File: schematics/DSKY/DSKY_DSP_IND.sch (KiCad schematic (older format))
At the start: 87 parts, among them Q10 Q_NPN, Q11 Q_NPN, Q12 Q_NPN, Q13 Q_NPN, Q14 Q_NPN, Q15 Q_NPN, Q16 Q_NPN, Q3 Q_NPN, Q4 Q_NPN, Q5 Q_NPN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

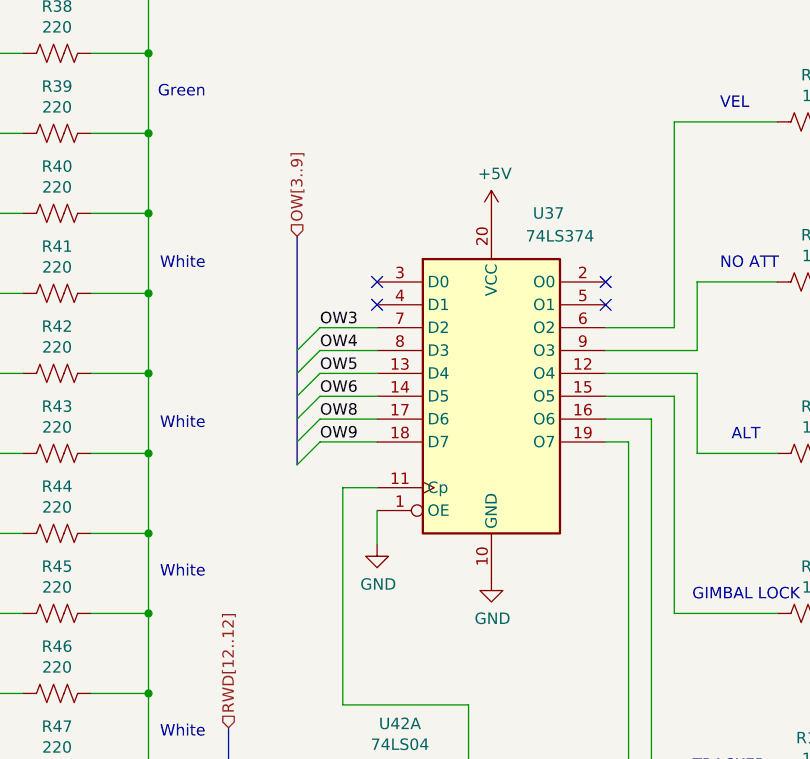
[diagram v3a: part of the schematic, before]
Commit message: Simplified reset lines.
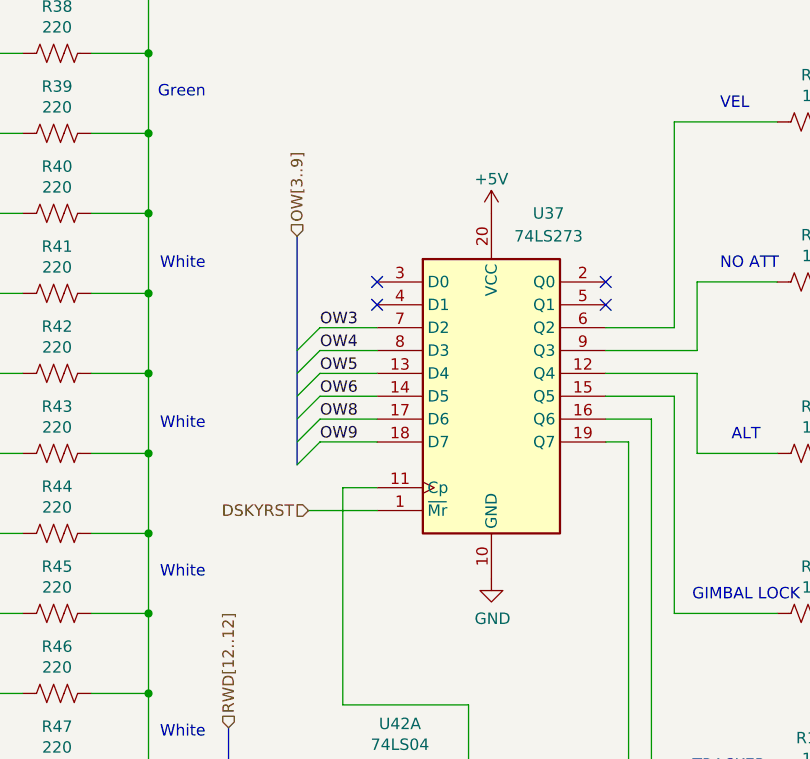
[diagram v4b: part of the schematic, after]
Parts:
- removed U37: 74LS374, symbol 74xx:74LS374
- added U37: 74LS273, symbol 74xx:74LS273
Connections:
- net +5V: now also U37.20 (VCC)
- net GND: now also U37.10 (GND)
- net OW3: now also U37.7 (D2)
- net OW4: now also U37.8 (D3)
- net OW5: now also U37.13 (D4)
- net OW6: now also U37.14 (D5)
- net OW8: now also U37.17 (D6)
- net OW9: now also U37.18 (D7)
- net PROG: now also U37.19 (Q7)
- net at U42.2: now also U37.11 (Cp)
- net at R8.1: now also U37.12 (Q4)
- net at R9.1: now also U37.15 (Q5)
- net at R10.1: now also U37.16 (Q6)
- net at R6.1: now also U37.6 (Q2)
- net at R7.1: now also U37.9 (Q3)
- new net DSKYRST: U37.1 (~Mr)
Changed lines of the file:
@@
 	1    0    0    -1
 $EndComp
-Wire Wire Line
-	6000 4000 6000 4150
 $Comp
 L power:+5V #PWR?
@@
 AR Path="/60F98A64/68A00B2E/68A8928A" Ref="#PWR0116"  Part="1"
 F 0 "#PWR0116" H 6500 2550 50  0001 C CNN
-F 1 "+5V" H 6515 2873 50  0000 C CNN
+F 1 "+5V" H 6500 2850 50  0000 C CNN
 F 2 "" H 6500 2700 50  0001 C CNN
 F 3 "" H 6500 2700 50  0001 C CNN
@@
 F 3 "" H 6500 4300 50  0001 C CNN
 	1    6500 4300
-	1    0    0    -1
-$EndComp
-$Comp
-L 74xx:74LS374 U?
-U 1 1 68A8927E
-P 6500 3500
-AR Path="/60F98A64/637944C1/68A8927E" Ref="U?"  Part="1"
-AR Path="/60F98A64/64844A8A/68A8927E" Ref="U?"  Part="1"
-AR Path="/60F98A64/63794472/68A8927E" Ref="U?"  Part="1"
-AR Path="/60F98A64/68A00B2E/68A8927E" Ref="U37"  Part="1"
-F 0 "U37" H 6750 4300 50  0000 C CNN
-F 1 "74LS374" H 6800 4200 50  0000 C CNN
-F 2 "" H 6500 3500 50  0001 C CNN
-F 3 "http://www.ti.com/lit/gpn/sn74LS374" H 6500 3500 50  0001 C CNN
-	1    6500 3500
 	1    0    0    -1
 $EndComp
@@
 NoConn ~ 6000 3100
 $Comp
-L power:GND #PWR?
-U 1 1 635E6D82
-P 6000 4150
-AR Path="/60F98A64/637944C1/635E6D82" Ref="#PWR?"  Part="1"
-AR Path="/60F98A64/64844A8A/635E6D82" Ref="#PWR?"  Part="1"
-AR Path="/60F98A64/63794472/635E6D82" Ref="#PWR?"  Part="1"
-AR Path="/60F98A64/68A00B2E/635E6D82" Ref="#PWR0110"  Part="1"
-F 0 "#PWR0110" H 6000 3900 50  0001 C CNN
-F 1 "GND" H 6005 3977 50  0000 C CNN
-F 2 "" H 6000 4150 50  0001 C CNN
-F 3 "" H 6000 4150 50  0001 C CNN
-	1    6000 4150
-	1    0    0    -1
-$EndComp
-$Comp
 L 74xx:74LS04 U42
 U 1 1 635EB464
@@
 Wire Wire Line
 	6400 4850 6400 5250
+$Comp
+L 74xx:74LS273 U37
+U 1 1 638DD418
+P 6500 3500
+F 0 "U37" H 6750 4300 50  0000 C CNN
+F 1 "74LS273" H 6750 4200 50  0000 C CNN
+F 2 "" H 6500 3500 50  0001 C CNN
+F 3 "http://www.ti.com/lit/gpn/sn74LS273" H 6500 3500 50  0001 C CNN
+	1    6500 3500
+	1    0    0    -1
+$EndComp
+Text HLabel 5700 4000 0    50   Input ~ 0
+DSKYRST
+Wire Wire Line
+	6000 4000 5700 4000
 Wire Bus Line
 	5350 4950 5350 5400

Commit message: Added DSKY test schematic
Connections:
- net PROG: no longer names the net of R11.1, U37.19 (Q7)
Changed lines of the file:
@@
 $Descr A 11000 8500
 encoding utf-8
-Sheet 5 11
+Sheet 5 12
 Title ""
 Date ""
@@
 Text Notes 2400 6600 2    50   ~ 0
 Flash V/N
-Wire Wire Line
-	7100 5900 7100 6150
-Wire Wire Line
-	7100 6150 7350 6150
-Connection ~ 7100 5900
-Text HLabel 7350 6150 2    50   Output ~ 0
-PROG
 NoConn ~ 7000 3000
 Connection ~ 10200 1950

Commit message: DSKY Redesign
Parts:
- removed D31, D32: LED, symbol Device:LED
- removed Q16: Q_NPN, symbol Device:Q_NPN_BCE
- removed R35: 1k, symbol Device:R_US
- removed R50, R51: 220, symbol Device:R_US
- added unit 3 of U19
- renumbered U42 to U19, U40 to U59
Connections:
- net PARALM: now also U59.13; no longer U59.1
- net STBY: now also U19.5; no longer U59.2
- net at R28.1: now also U59.11; no longer U59.3
- new net: U19.6, U59.12
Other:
- note removed: "Flash V/N"
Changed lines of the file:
@@
 $Descr A 11000 8500
 encoding utf-8
-Sheet 5 12
+Sheet 7 15
 Title ""
 Date ""
@@
 Text Notes 5050 5700 0    50   ~ 0
 Yellow
-$Comp
-L Device:Q_NPN_BCE Q?
-U 1 1 66B1B9DB
-P 3250 6650
-AR Path="/60F98A64/64844A8A/66B1B9DB" Ref="Q?"  Part="1"
-AR Path="/60F98A64/68A00B2E/66B1B9DB" Ref="Q16"  Part="1"
-F 0 "Q16" H 3441 6696 50  0000 L CNN
-F 1 "Q_NPN" H 3441 6605 50  0000 L CNN
-F 2 "" H 3450 6750 50  0001 C CNN
-F 3 "~" H 3250 6650 50  0001 C CNN
-	1    3250 6650
-	1    0    0    -1
-$EndComp
-$Comp
-L Device:R_US R?
-U 1 1 66B1B9E1
-P 2700 6650
-AR Path="/60F98A64/64844A8A/66B1B9E1" Ref="R?"  Part="1"
-AR Path="/60F98A64/68A00B2E/66B1B9E1" Ref="R35"  Part="1"
-F 0 "R35" V 2905 6650 50  0000 C CNN
-F 1 "1k" V 2814 6650 50  0000 C CNN
-F 2 "" V 2740 6640 50  0001 C CNN
-F 3 "~" H 2700 6650 50  0001 C CNN
-	1    2700 6650
-	0    -1   -1   0
-$EndComp
-$Comp
-L Device:LED D?
-U 1 1 66B1B9E7
-P 4150 6250
-AR Path="/60F98A64/64844A8A/66B1B9E7" Ref="D?"  Part="1"
-AR Path="/60F98A64/68A00B2E/66B1B9E7" Ref="D31"  Part="1"
-F 0 "D31" H 4143 6467 50  0000 C CNN
-F 1 "LED" H 4143 6376 50  0000 C CNN
-F 2 "" H 4150 6250 50  0001 C CNN
-F 3 "~" H 4150 6250 50  0001 C CNN
-	1    4150 6250
-	1    0    0    -1
-$EndComp
-$Comp
-L Device:LED D?
-U 1 1 66B1B9ED
-P 4150 6650
-AR Path="/60F98A64/64844A8A/66B1B9ED" Ref="D?"  Part="1"
-AR Path="/60F98A64/68A00B2E/66B1B9ED" Ref="D32"  Part="1"
-F 0 "D32" H 4143 6867 50  0000 C CNN
-F 1 "LED" H 4143 6776 50  0000 C CNN
-F 2 "" H 4150 6650 50  0001 C CNN
-F 3 "~" H 4150 6650 50  0001 C CNN
-	1    4150 6650
-	1    0    0    -1
-$EndComp
-$Comp
-L Device:R_US R?
-U 1 1 66B1B9F3
-P 4600 6250
-AR Path="/60F98A64/64844A8A/66B1B9F3" Ref="R?"  Part="1"
-AR Path="/60F98A64/68A00B2E/66B1B9F3" Ref="R50"  Part="1"
-F 0 "R50" V 4805 6250 50  0000 C CNN
-F 1 "220" V 4714 6250 50  0000 C CNN
-F 2 "" V 4640 6240 50  0001 C CNN
-F 3 "~" H 4600 6250 50  0001 C CNN
-	1    4600 6250
-	0    -1   -1   0
-$EndComp
-$Comp
-L Device:R_US R?
-U 1 1 66B1B9F9
-P 4600 6650
-AR Path="/60F98A64/64844A8A/66B1B9F9" Ref="R?"  Part="1"
-AR Path="/60F98A64/68A00B2E/66B1B9F9" Ref="R51"  Part="1"
-F 0 "R51" V 4805 6650 50  0000 C CNN
-F 1 "220" V 4714 6650 50  0000 C CNN
-F 2 "" V 4640 6640 50  0001 C CNN
-F 3 "~" H 4600 6650 50  0001 C CNN
-	1    4600 6650
-	0    -1   -1   0
-$EndComp
-$Comp
-L power:GND #PWR?
-U 1 1 66B1B9FF
-P 3350 6850
-AR Path="/60F98A64/64844A8A/66B1B9FF" Ref="#PWR?"  Part="1"
-AR Path="/60F98A64/68A00B2E/66B1B9FF" Ref="#PWR0189"  Part="1"
-F 0 "#PWR0189" H 3350 6600 50  0001 C CNN
-F 1 "GND" H 3355 6677 50  0000 C CNN
-F 2 "" H 3350 6850 50  0001 C CNN
-F 3 "" H 3350 6850 50  0001 C CNN
-	1    3350 6850
-	1    0    0    -1
-$EndComp
-Wire Wire Line
-	4450 6650 4300 6650
-Wire Wire Line
-	4450 6250 4300 6250
-Wire Wire Line
-	4750 6650 5000 6650
-Wire Wire Line
-	5000 6650 5000 6250
-Wire Wire Line
-	4750 6250 5000 6250
-Connection ~ 5000 6250
-Wire Wire Line
-	5000 6250 5000 5900
-Wire Wire Line
-	2850 6650 3050 6650
-Wire Wire Line
-	4000 6250 3850 6250
-Wire Wire Line
-	3850 6250 3850 6450
-Wire Wire Line
-	3850 6650 4000 6650
-Wire Wire Line
-	3350 6450 3850 6450
-Connection ~ 3850 6450
-Wire Wire Line
-	3850 6450 3850 6650
-Text HLabel 1500 1550 0    50   Input ~ 0
+Text HLabel 1500 1750 0    50   Input ~ 0
 PARALM
-Text Notes 5050 6450 0    50   ~ 0
-Green
-Connection ~ 5000 5900
 Entry Wire Line
 	950  3150 1050 3050
@@
 Wire Wire Line
 	1050 3750 2550 3750
-Text HLabel 1500 1750 0    50   Input ~ 0
+Text HLabel 900  1550 0    50   Input ~ 0
 STBY
 $Comp
-L 74xx:74LS32 U40
-U 1 1 609B0A05
+L 74xx:74LS32 U59
+U 4 1 609B0A05
 P 1800 1650
-F 0 "U40" H 1800 1975 50  0000 C CNN
+F 0 "U59" H 1800 1975 50  0000 C CNN
 F 1 "74LS32" H 1800 1884 50  0000 C CNN
 F 2 "" H 1800 1650 50  0001 C CNN
 F 3 "http://www.ti.com/lit/gpn/sn74LS32" H 1800 1650 50  0001 C CNN
-	1    1800 1650
-	1    0    0    -1
-$EndComp
-Wire Wire Line
-	1050 6650 2550 6650
-Entry Wire Line
-	950  6750 1050 6650
-Text Label 1050 6650 0    50   ~ 0
-IND6
-Text Notes 2400 6600 2    50   ~ 0
-Flash V/N
+	4    1800 1650
+	1    0    0    -1
+$EndComp
 NoConn ~ 7000 3000
 Connection ~ 10200 1950
@@
 NoConn ~ 6000 3100
 $Comp
-L 74xx:74LS04 U42
+L 74xx:74LS04 U19
 U 1 1 635EB464
 P 6100 5250
-F 0 "U42" H 6100 5567 50  0000 C CNN
+F 0 "U19" H 6100 5567 50  0000 C CNN
 F 1 "74LS04" H 6100 5476 50  0000 C CNN
 F 2 "" H 6100 5250 50  0001 C CNN
@@
 	5650 2800 5650 3800
 Wire Bus Line
-	950  2000 950  6900
+	950  2000 950  6100
+$Comp
+L 74xx:74LS04 U19
+U 3 1 6A128701
+P 1200 1550
+F 0 "U19" H 1200 1867 50  0000 C CNN
+F 1 "74LS04" H 1200 1776 50  0000 C CNN
+F 2 "" H 1200 1550 50  0001 C CNN
+F 3 "http://www.ti.com/lit/gpn/sn74LS04" H 1200 1550 50  0001 C CNN
+	3    1200 1550
+	1    0    0    -1
+$EndComp
 $EndSCHEMATC

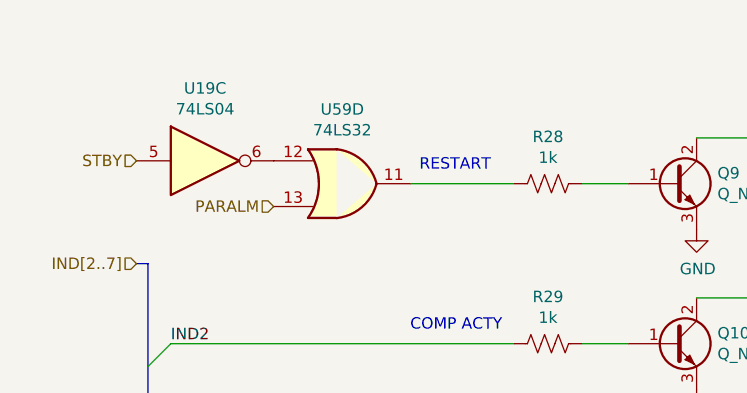
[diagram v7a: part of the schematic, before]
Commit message: Using 4 LED driver chips.
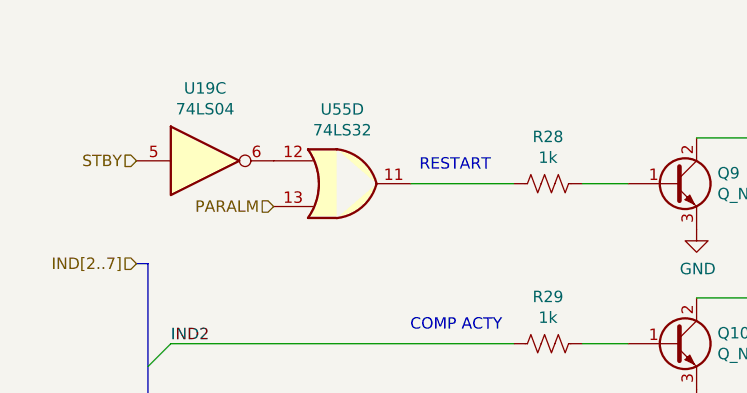
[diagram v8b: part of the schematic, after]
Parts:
- renumbered U59 to U55
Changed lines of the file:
@@
 $Descr A 11000 8500
 encoding utf-8
-Sheet 7 15
+Sheet 5 13
 Title ""
 Date ""
@@
 	9650 5900 9500 5900
 $Comp
-L power:GND #PWR0126
+L power:GND #PWR0153
 U 1 1 68ACC778
 P 8550 6100
-F 0 "#PWR0126" H 8550 5850 50  0001 C CNN
+F 0 "#PWR0153" H 8550 5850 50  0001 C CNN
 F 1 "GND" H 8555 5927 50  0000 C CNN
 F 2 "" H 8550 6100 50  0001 C CNN
@@
 $EndComp
 $Comp
-L power:GND #PWR0125
+L power:GND #PWR0154
 U 1 1 68ACC772
 P 8550 5400
-F 0 "#PWR0125" H 8550 5150 50  0001 C CNN
+F 0 "#PWR0154" H 8550 5150 50  0001 C CNN
 F 1 "GND" H 8555 5227 50  0000 C CNN
 F 2 "" H 8550 5400 50  0001 C CNN
@@
 	9650 4450 9500 4450
 $Comp
-L power:GND #PWR0124
+L power:GND #PWR0155
 U 1 1 68AB7385
 P 8550 4650
-F 0 "#PWR0124" H 8550 4400 50  0001 C CNN
+F 0 "#PWR0155" H 8550 4400 50  0001 C CNN
 F 1 "GND" H 8555 4477 50  0000 C CNN
 F 2 "" H 8550 4650 50  0001 C CNN
@@
 $EndComp
 $Comp
-L power:GND #PWR0123
+L power:GND #PWR0156
 U 1 1 68AB737F
 P 8550 3950
-F 0 "#PWR0123" H 8550 3700 50  0001 C CNN
+F 0 "#PWR0156" H 8550 3700 50  0001 C CNN
 F 1 "GND" H 8555 3777 50  0000 C CNN
 F 2 "" H 8550 3950 50  0001 C CNN
@@
 	9650 3000 9500 3000
 $Comp
-L power:GND #PWR0122
+L power:GND #PWR0157
 U 1 1 68AA0FA2
 P 8550 3200
-F 0 "#PWR0122" H 8550 2950 50  0001 C CNN
+F 0 "#PWR0157" H 8550 2950 50  0001 C CNN
 F 1 "GND" H 8555 3027 50  0000 C CNN
 F 2 "" H 8550 3200 50  0001 C CNN
@@
 $EndComp
 $Comp
-L power:GND #PWR0121
+L power:GND #PWR0158
 U 1 1 68AA0F9C
 P 8550 2500
-F 0 "#PWR0121" H 8550 2250 50  0001 C CNN
+F 0 "#PWR0158" H 8550 2250 50  0001 C CNN
 F 1 "GND" H 8555 2327 50  0000 C CNN
 F 2 "" H 8550 2500 50  0001 C CNN
@@
 STBY
 $Comp
-L 74xx:74LS32 U59
+L 74xx:74LS32 U55
 U 4 1 609B0A05
 P 1800 1650
-F 0 "U59" H 1800 1975 50  0000 C CNN
+F 0 "U55" H 1800 1975 50  0000 C CNN
 F 1 "74LS32" H 1800 1884 50  0000 C CNN
 F 2 "" H 1800 1650 50  0001 C CNN
@@
 Wire Wire Line
 	6000 4000 5700 4000
+$Comp
+L 74xx:74LS04 U19
+U 3 1 6E8434D9
+P 1200 1550
+F 0 "U19" H 1200 1867 50  0000 C CNN
+F 1 "74LS04" H 1200 1776 50  0000 C CNN
+F 2 "" H 1200 1550 50  0001 C CNN
+F 3 "http://www.ti.com/lit/gpn/sn74LS04" H 1200 1550 50  0001 C CNN
+	3    1200 1550
+	1    0    0    -1
+$EndComp
 Wire Bus Line
 	5350 4950 5350 5400
@@
 Wire Bus Line
 	950  2000 950  6100
-$Comp
-L 74xx:74LS04 U19
-U 3 1 6A128701
-P 1200 1550
-F 0 "U19" H 1200 1867 50  0000 C CNN
-F 1 "74LS04" H 1200 1776 50  0000 C CNN
-F 2 "" H 1200 1550 50  0001 C CNN
-F 3 "http://www.ti.com/lit/gpn/sn74LS04" H 1200 1550 50  0001 C CNN
-	3    1200 1550
-	1    0    0    -1
-$EndComp
 $EndSCHEMATC
